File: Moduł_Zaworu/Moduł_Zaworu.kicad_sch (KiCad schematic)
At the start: 8 parts, among them J2 RJ45, J3 RJ45, J8 Screw_Terminal_01x02, U11 ESP32-DEVKITC

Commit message: Gotowy do zatwierdzenia moduł zasilaina
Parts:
- renumbered J8 to J2, J2 to J3, J3 to J4, R13 to R10, R15 to R4, R12 to R5, R14 to R9, U11 to U6
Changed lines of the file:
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@@
 		(dnp no)
 		(fields_autoplaced yes)
-		(property "Reference" "R15"
+		(property "Reference" "R4"
 			(at 217.17 130.8099 0)
 			(effects
@@
 			(project "Moduł_Zaworu"
 				(path "/8513fd68-b07b-4062-94bb-7b0327ec704f"
-					(reference "R15")
+					(reference "R4")
 					(unit 1)
 				)
@@
 		(dnp no)
 		(fields_autoplaced yes)
-		(property "Reference" "J8"
+		(property "Reference" "J2"
 			(at 138.43 55.8799 0)
 			(effects
@@
 			(project ""
 				(path "/8513fd68-b07b-4062-94bb-7b0327ec704f"
-					(reference "J8")
+					(reference "J2")
 					(unit 1)
 				)
@@
 		(dnp no)
 		(fields_autoplaced yes)
-		(property "Reference" "U11"
+		(property "Reference" "U6"
 			(at 100.33 38.1 0)
 			(effects
@@
 			(project "Moduł_Zaworu"
 				(path "/8513fd68-b07b-4062-94bb-7b0327ec704f"
-					(reference "U11")
+					(reference "U6")
 					(unit 1)
 				)
@@
 		(on_board yes)
 		(dnp no)
-		(property "Reference" "R13"
+		(property "Reference" "R10"
 			(at 160.02 143.5099 0)
 			(effects
@@
 			(project "Moduł_Zaworu"
 				(path "/8513fd68-b07b-4062-94bb-7b0327ec704f"
-					(reference "R13")
+					(reference "R10")
 					(unit 1)
 				)
@@
 		(on_board yes)
 		(dnp no)
-		(property "Reference" "R12"
+		(property "Reference" "R5"
 			(at 207.01 130.8099 0)
 			(effects
@@
 			(project "Moduł_Zaworu"
 				(path "/8513fd68-b07b-4062-94bb-7b0327ec704f"
-					(reference "R12")
+					(reference "R5")
 					(unit 1)
 				)
@@
 		(dnp no)
 		(fields_autoplaced yes)
-		(property "Reference" "J3"
+		(property "Reference" "J4"
 			(at 125.73 130.81 0)
 			(effects
@@
 			(project "Moduł_Zaworu"
 				(path "/8513fd68-b07b-4062-94bb-7b0327ec704f"
-					(reference "J3")
+					(reference "J4")
 					(unit 1)
 				)
@@
 		(dnp no)
 		(fields_autoplaced yes)
-		(property "Reference" "R14"
+		(property "Reference" "R9"
 			(at 160.02 153.6699 0)
 			(effects
@@
 			(project "Moduł_Zaworu"
 				(path "/8513fd68-b07b-4062-94bb-7b0327ec704f"
-					(reference "R14")
+					(reference "R9")
 					(unit 1)
 				)
@@
 		(dnp no)
 		(fields_autoplaced yes)
-		(property "Reference" "J2"
+		(property "Reference" "J3"
 			(at 52.07 133.35 0)
 			(effects
@@
 			(project "Moduł_Zaworu"
 				(path "/8513fd68-b07b-4062-94bb-7b0327ec704f"
-					(reference "J2")
-					(unit 1)
-				)
+					(reference "J3")
+					(unit 1)
+				)

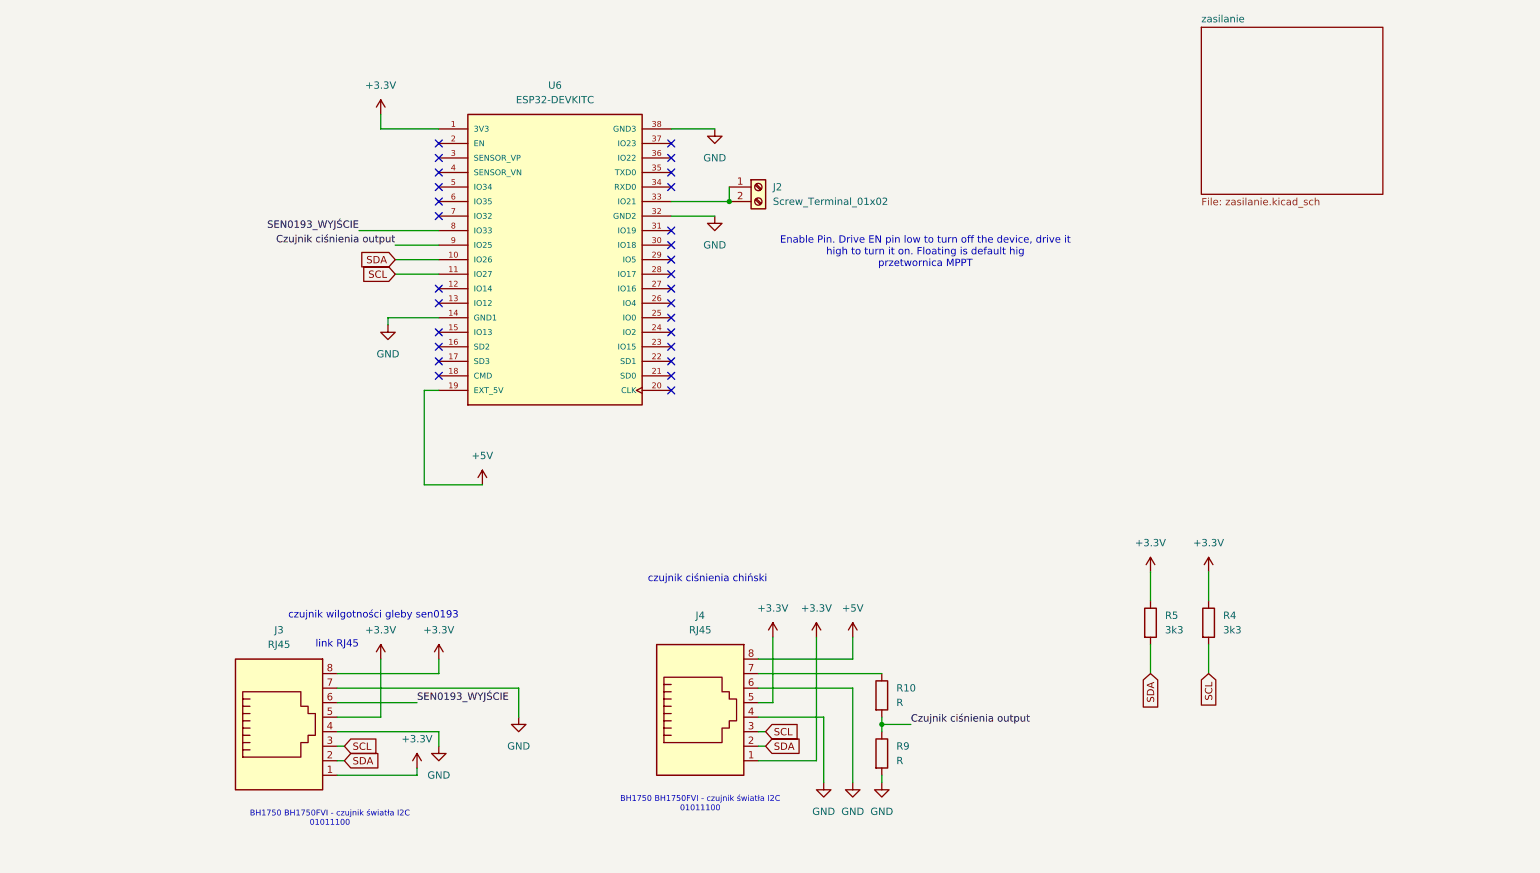
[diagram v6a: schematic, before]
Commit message: Kod websocket, kod stonka demo, kod sterownika - wszystkie taski poza bt wstepnie ogarniete
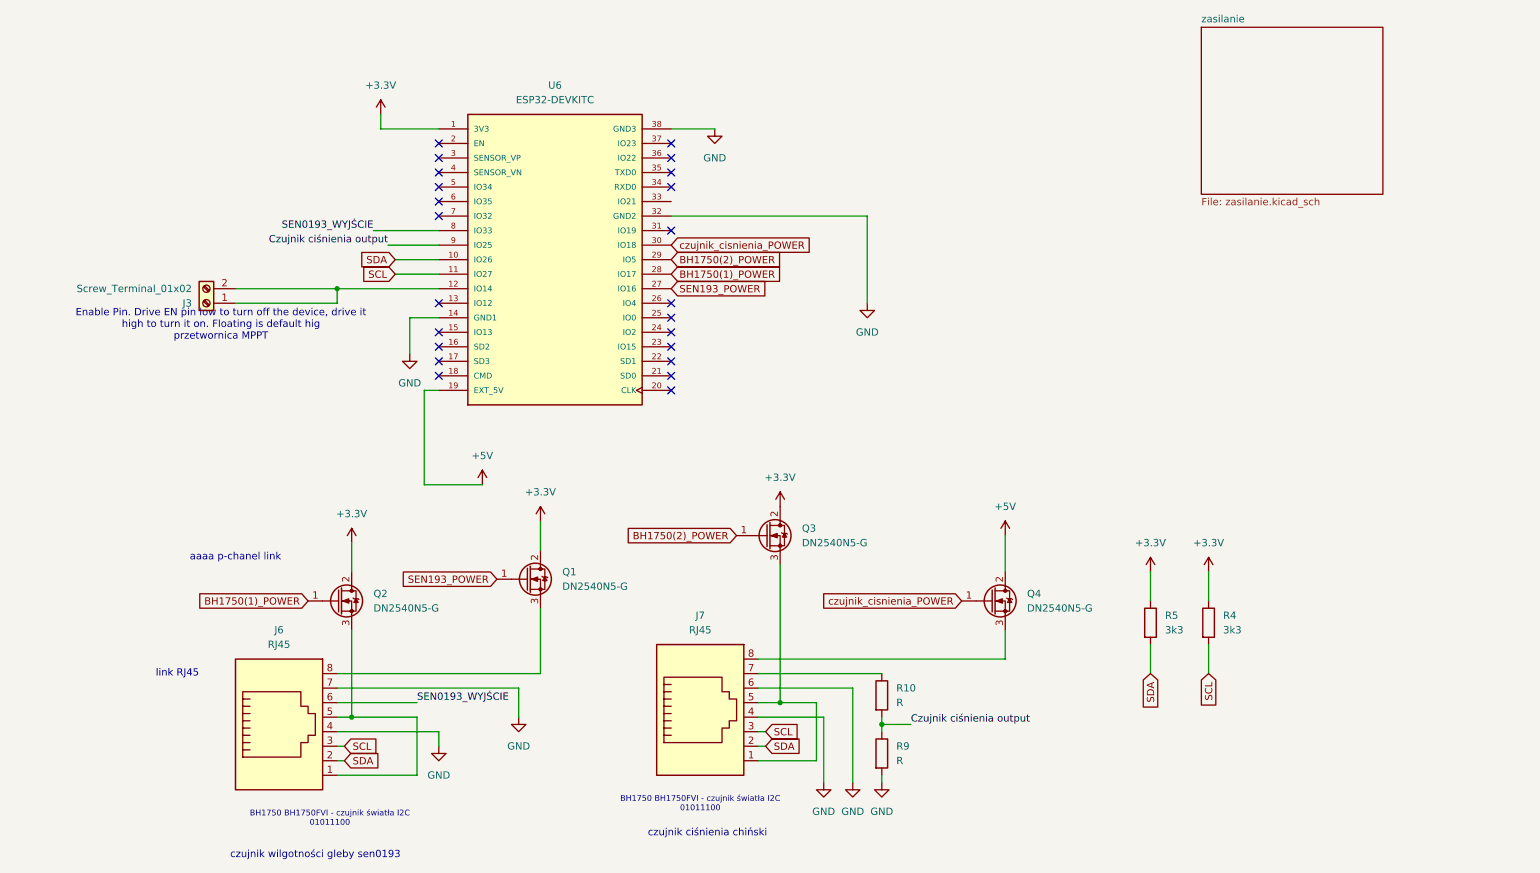
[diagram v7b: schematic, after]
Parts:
- added Q1, Q2, Q3, Q4: DN2540N5-G, Package_TO_SOT_SMD:SOT-23_Handsoldering, symbol Transistor_FET_Other:DN2540N5-G
- renumbered J2 to J3, J3 to J6, J4 to J7
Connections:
- net +3.3V: now also Q1.2 (D), Q2.2 (D), Q3.2 (D); no longer J6.1, J6.5, J6.8, J7.1, J7.5
- net +5V: now also Q4.2 (D); no longer J7.8
- net at J3.1 (Pin_1), J3.2 (Pin_2): now also U6.12 (IO14); no longer U6.33 (IO21)
- net SEN193_POWER: now reaches U6.27 (IO16)
- net SEN193_POWER: now also Q1.1 (G)
- net BH1750(1)_POWER: now reaches U6.28 (IO17)
- net BH1750(1)_POWER: now also Q2.1 (G)
- net BH1750(2)_POWER: now reaches U6.29 (IO5)
- net BH1750(2)_POWER: now also Q3.1 (G)
- net czujnik_cisnienia_POWER: now reaches U6.30 (IO18)
- net czujnik_cisnienia_POWER: now also Q4.1 (G)
- new net: J6.8, Q1.3 (S)
- new net: J6.1, J6.5, Q2.3 (S)
- new net: J7.1, J7.5, Q3.3 (S)
- new net: J7.8, Q4.3 (S)
- no-connect marks 28 -> 23
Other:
- note added: "aaaa p-chanel link"
- moved on the sheet: J3
